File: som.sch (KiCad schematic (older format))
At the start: 21 parts, among them J7 MC-HVT1-S04-G, M1 SA800U-WF-mechanical_model, U10 SA800U-WF

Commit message: Add footprint to SoM mechanical model
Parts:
- M1: footprint (none) -> sa800u-baseboard-hw-footprints:SA800U-WF_mechanical_model
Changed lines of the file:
@@
 F 0 "M1" H 15400 975 50  0000 C CNN
 F 1 "SA800U-WF-mechanical_model" H 15400 800 50  0000 C CNN
-F 2 "" H 15400 800 50  0001 C CNN
+F 2 "sa800u-baseboard-hw-footprints:SA800U-WF_mechanical_model" H 15400 800 50  0001 C CNN
 F 3 "" H 15400 800 50  0001 C CNN
 	1    15400 800

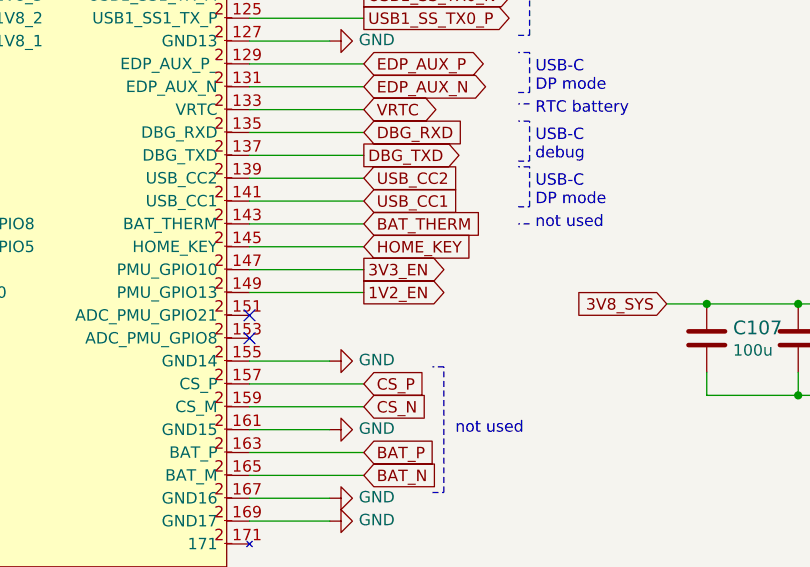
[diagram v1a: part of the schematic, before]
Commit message: Add 47k resistor to BAT_THERM
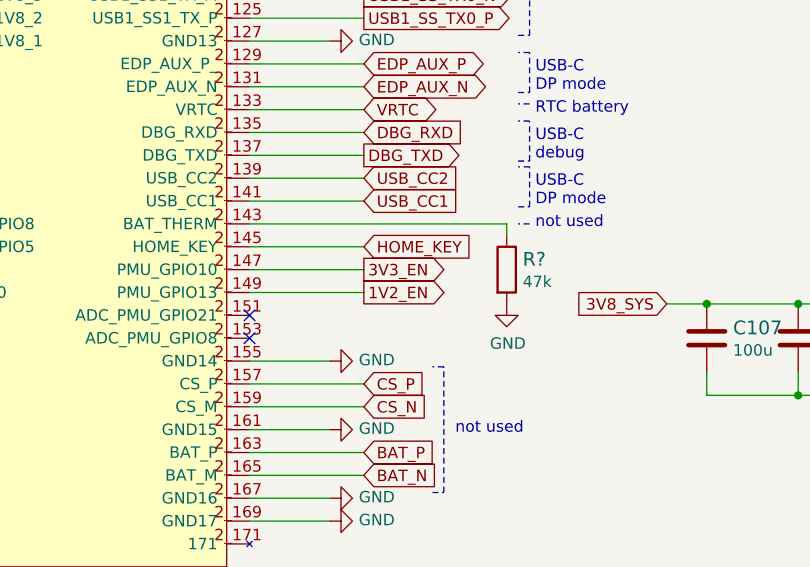
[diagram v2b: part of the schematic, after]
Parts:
- added R?: R_47k_0402, antmicro-footprints:0402-res, symbol antmicroResistors0402:R_47k_0402
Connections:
- net GND: now also R?.2
- net BAT_THERM: no longer names the net of U10.2_143 (BAT_THERM)
- net BAT_THERM: now also R?.1
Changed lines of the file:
@@
 Text GLabel 10250 8500 2    50   Input ~ 0
 USB_CC1
-Text GLabel 10250 8600 2    50   Input ~ 0
-BAT_THERM
 Text GLabel 10250 8700 2    50   Input ~ 0
 HOME_KEY
@@
 Wire Wire Line
 	10250 8700 9750 8700
-Wire Wire Line
-	10250 8600 9750 8600
 Wire Wire Line
 	10250 8500 9750 8500
@@
 Wire Wire Line
 	14450 8950 14450 8975
+$Comp
+L antmicroResistors0402:R_47k_0402 R?
+U 1 1 6208BD31
+P 10875 8800
+F 0 "R?" V 10830 8870 60  0000 L CNN
+F 1 "R_47k_0402" H 10875 8650 60  0001 C CNN
+F 2 "antmicro-footprints:0402-res" H 11075 9000 60  0001 L CNN
+F 3 "" H 10875 8800 50  0001 C CNN
+F 4 "MULTICOMP" H 11075 9200 60  0001 L CNN "Manufacturer"
+F 5 "MCMR04X4702FTL" H 11075 9100 60  0001 L CNN "MPN"
+F 6 "47k" V 10928 8870 50  0000 L CNN "Val"
+	1    10875 8800
+	0    1    1    0
+$EndComp
+$Comp
+L sa800u-baseboard-hw:GND #PWR?
+U 1 1 6209423C
+P 10875 8950
+F 0 "#PWR?" H 10875 8700 50  0001 C CNN
+F 1 "GND" H 10880 8777 50  0000 C CNN
+F 2 "" H 10875 8950 50  0001 C CNN
+F 3 "" H 10875 8950 50  0001 C CNN
+	1    10875 8950
+	1    0    0    -1
+$EndComp
+Wire Wire Line
+	10875 8600 10875 8650
+Wire Wire Line
+	9750 8600 10875 8600
 $EndSCHEMATC

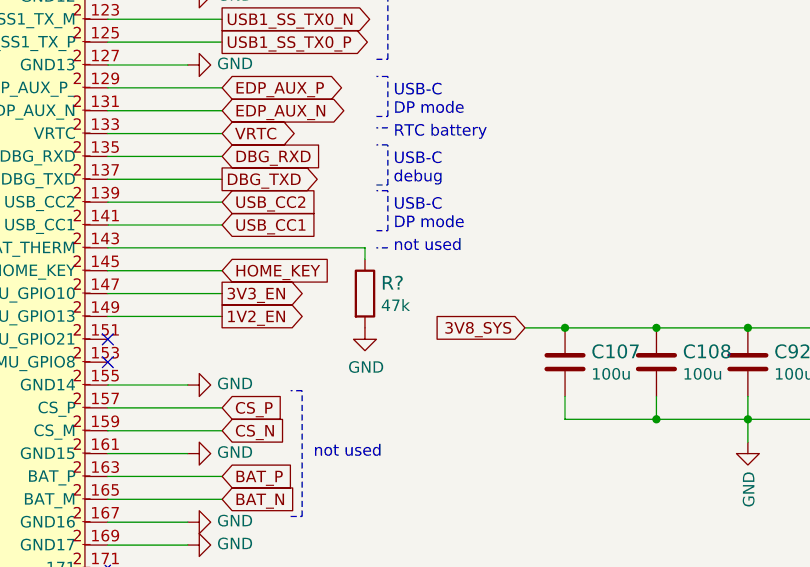
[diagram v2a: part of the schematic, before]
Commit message: Annotate BAT_THER resistor
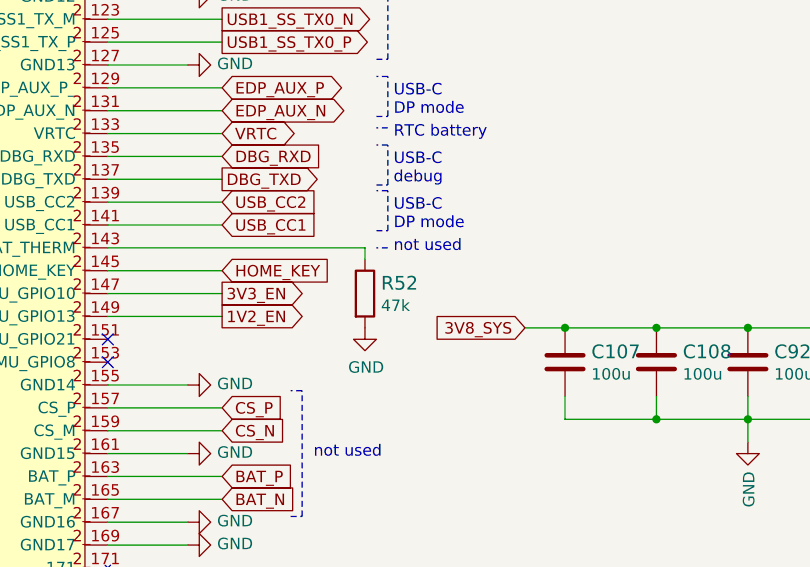
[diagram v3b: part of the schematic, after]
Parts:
- gave numbers to parts that had none: 1
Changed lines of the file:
@@
 	14450 8950 14450 8975
 $Comp
-L antmicroResistors0402:R_47k_0402 R?
+L antmicroResistors0402:R_47k_0402 R52
 U 1 1 6208BD31
 P 10875 8800
-F 0 "R?" V 10830 8870 60  0000 L CNN
+F 0 "R52" V 10830 8870 60  0000 L CNN
 F 1 "R_47k_0402" H 10875 8650 60  0001 C CNN
 F 2 "antmicro-footprints:0402-res" H 11075 9000 60  0001 L CNN
@@
 $EndComp
 $Comp
-L sa800u-baseboard-hw:GND #PWR?
+L sa800u-baseboard-hw:GND #PWR0246
 U 1 1 6209423C
 P 10875 8950
-F 0 "#PWR?" H 10875 8700 50  0001 C CNN
+F 0 "#PWR0246" H 10875 8700 50  0001 C CNN
 F 1 "GND" H 10880 8777 50  0000 C CNN
 F 2 "" H 10875 8950 50  0001 C CNN

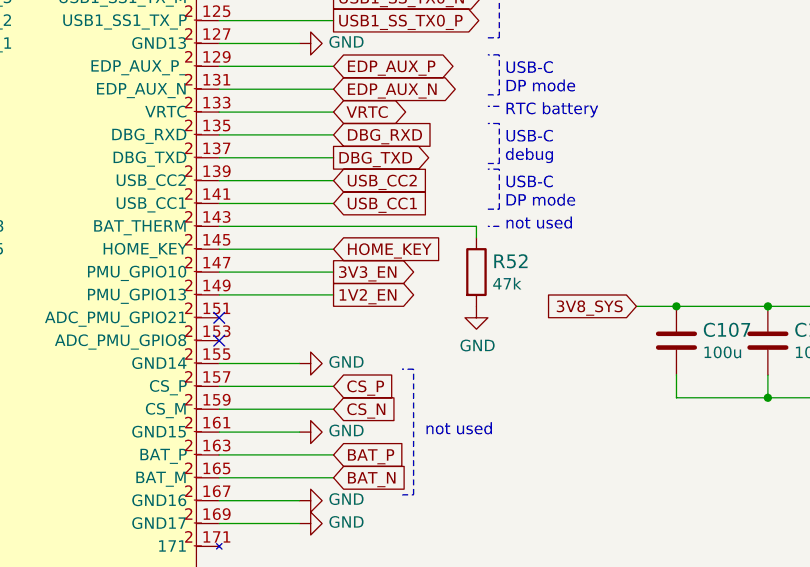
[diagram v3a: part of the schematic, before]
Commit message: Fix labels on GPIO controlling 3V3 and 1V2
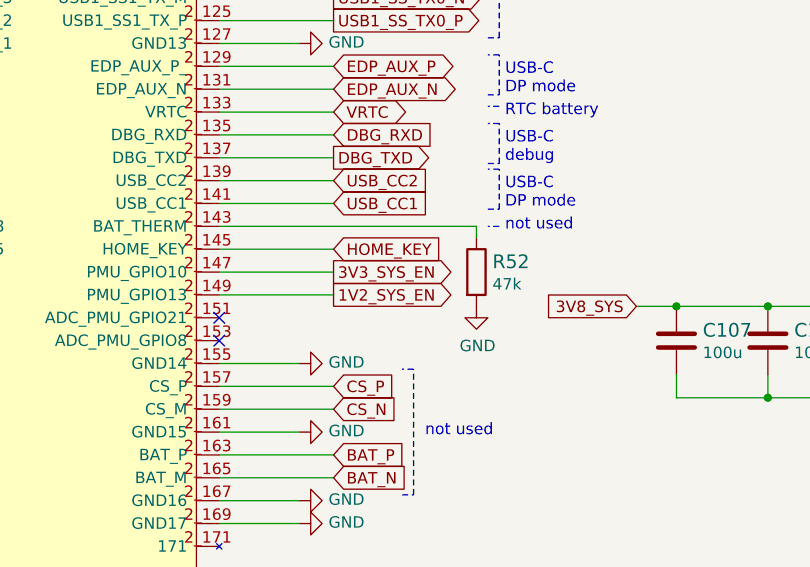
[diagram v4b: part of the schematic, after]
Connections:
- net 1V2_EN renamed 1V2_SYS_EN
- net 3V3_EN renamed 3V3_SYS_EN
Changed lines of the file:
@@
 	9750 8800 10250 8800
 Text GLabel 10250 8800 2    50   Output ~ 0
-3V3_EN
+3V3_SYS_EN
 Wire Wire Line
 	9750 8900 10250 8900
 Text GLabel 10250 8900 2    50   Output ~ 0
-1V2_EN
+1V2_SYS_EN
 Text GLabel 11575 8950 0    50   Input ~ 0
 3V8_SYS

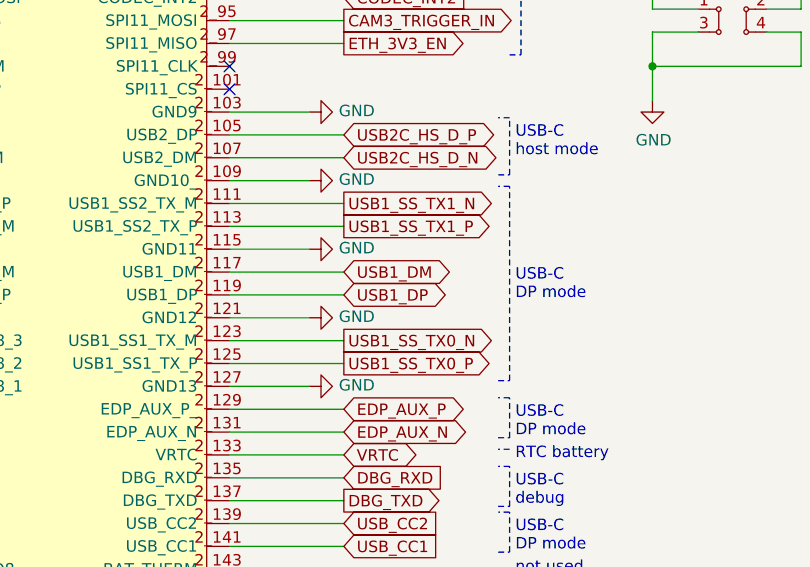
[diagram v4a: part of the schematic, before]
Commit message: Fix labels, fix p-mosfet symbol
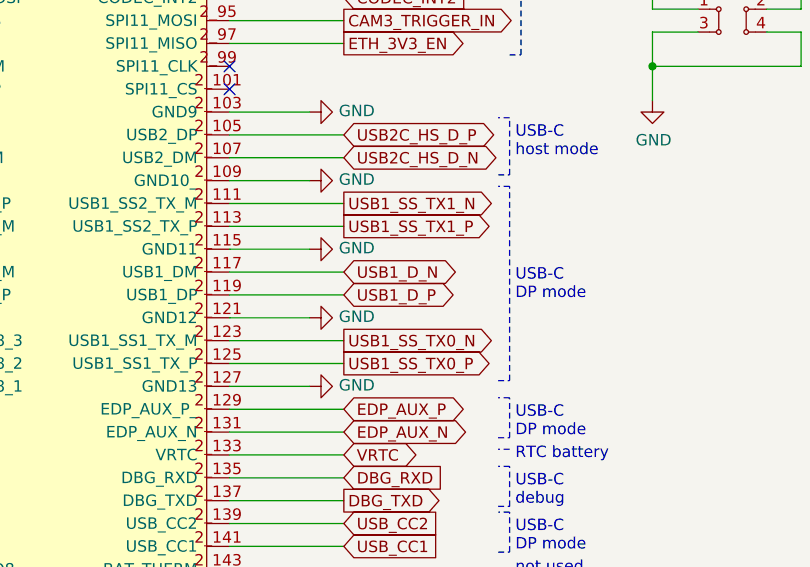
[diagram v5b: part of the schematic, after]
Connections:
- net USB1_DM renamed USB1_D_N
- net USB1_DP renamed USB1_D_P
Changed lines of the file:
@@
 Text GLabel 10250 7100 2    50   Output ~ 0
 USB1_SS_TX1_P
-Text GLabel 10250 7300 2    50   BiDi ~ 0
-USB1_DM
-Text GLabel 10250 7400 2    50   BiDi ~ 0
-USB1_DP
 Text GLabel 10250 7600 2    50   Output ~ 0
 USB1_SS_TX0_N
@@
 Wire Wire Line
 	9750 8600 10875 8600
+Text GLabel 10250 7300 2    50   BiDi ~ 0
+USB1_D_N
+Text GLabel 10250 7400 2    50   BiDi ~ 0
+USB1_D_P
 $EndSCHEMATC

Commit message: Loclib
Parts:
- R52: footprint antmicro-footprints:0402-res -> sa800u-baseboard-hw-footprints:0402-res; symbol antmicroResistors0402:R_47k_0402 -> sa800u-baseboard-hw:R_47k_0402
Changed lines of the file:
@@
 	14450 8950 14450 8975
 $Comp
-L antmicroResistors0402:R_47k_0402 R52
+L sa800u-baseboard-hw:R_47k_0402 R52
 U 1 1 6208BD31
 P 10875 8800
 F 0 "R52" V 10830 8870 60  0000 L CNN
 F 1 "R_47k_0402" H 10875 8650 60  0001 C CNN
-F 2 "antmicro-footprints:0402-res" H 11075 9000 60  0001 L CNN
+F 2 "sa800u-baseboard-hw-footprints:0402-res" H 11075 9000 60  0001 L CNN
 F 3 "" H 10875 8800 50  0001 C CNN
 F 4 "MULTICOMP" H 11075 9200 60  0001 L CNN "Manufacturer"

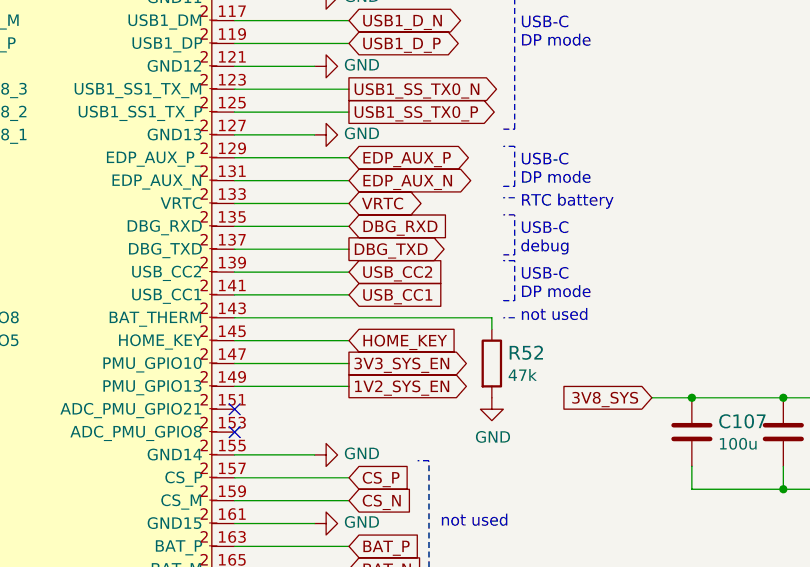
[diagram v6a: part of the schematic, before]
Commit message: Fix connection of CC1 and CC2 signals to som (global and local labels mixed)
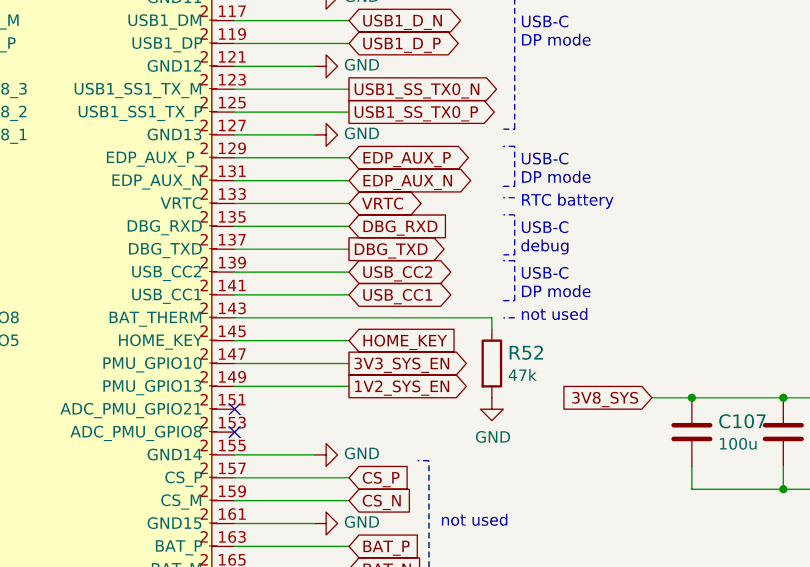
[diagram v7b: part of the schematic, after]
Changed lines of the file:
@@
 Text GLabel 10250 8300 2    50   Output ~ 0
 DBG_TXD
-Text GLabel 10250 8400 2    50   Input ~ 0
+Text GLabel 10250 8400 2    50   BiDi ~ 0
 USB_CC2
-Text GLabel 10250 8500 2    50   Input ~ 0
+Text GLabel 10250 8500 2    50   BiDi ~ 0
 USB_CC1
 Text GLabel 10250 8700 2    50   Input ~ 0

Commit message: Continue layout
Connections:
- no-connect marks 58 -> 54
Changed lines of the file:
@@
 NoConn ~ 8100 4400
 NoConn ~ 8100 4500
-NoConn ~ 8100 4600
-NoConn ~ 8100 4700
-NoConn ~ 8100 5000
-NoConn ~ 8100 5100
 Wire Wire Line
 	4150 8925 4525 8925
